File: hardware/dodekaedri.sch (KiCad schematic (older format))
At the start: 0 parts

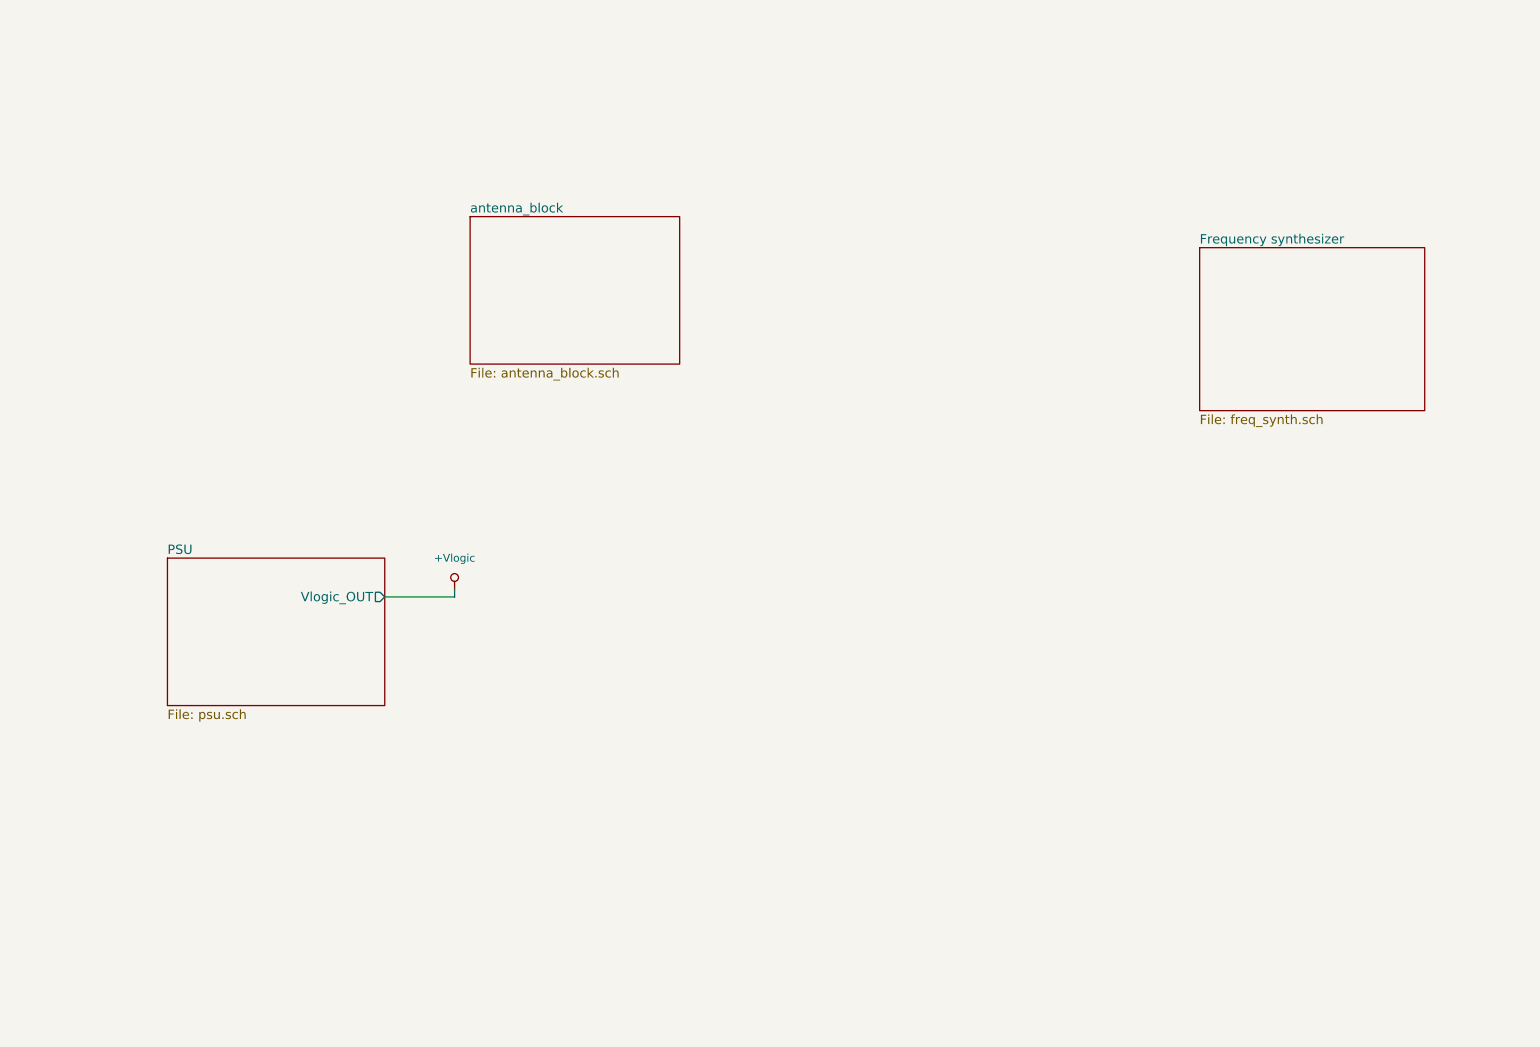
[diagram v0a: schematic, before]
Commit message: added rx/tx wm8731 (adc/dac)
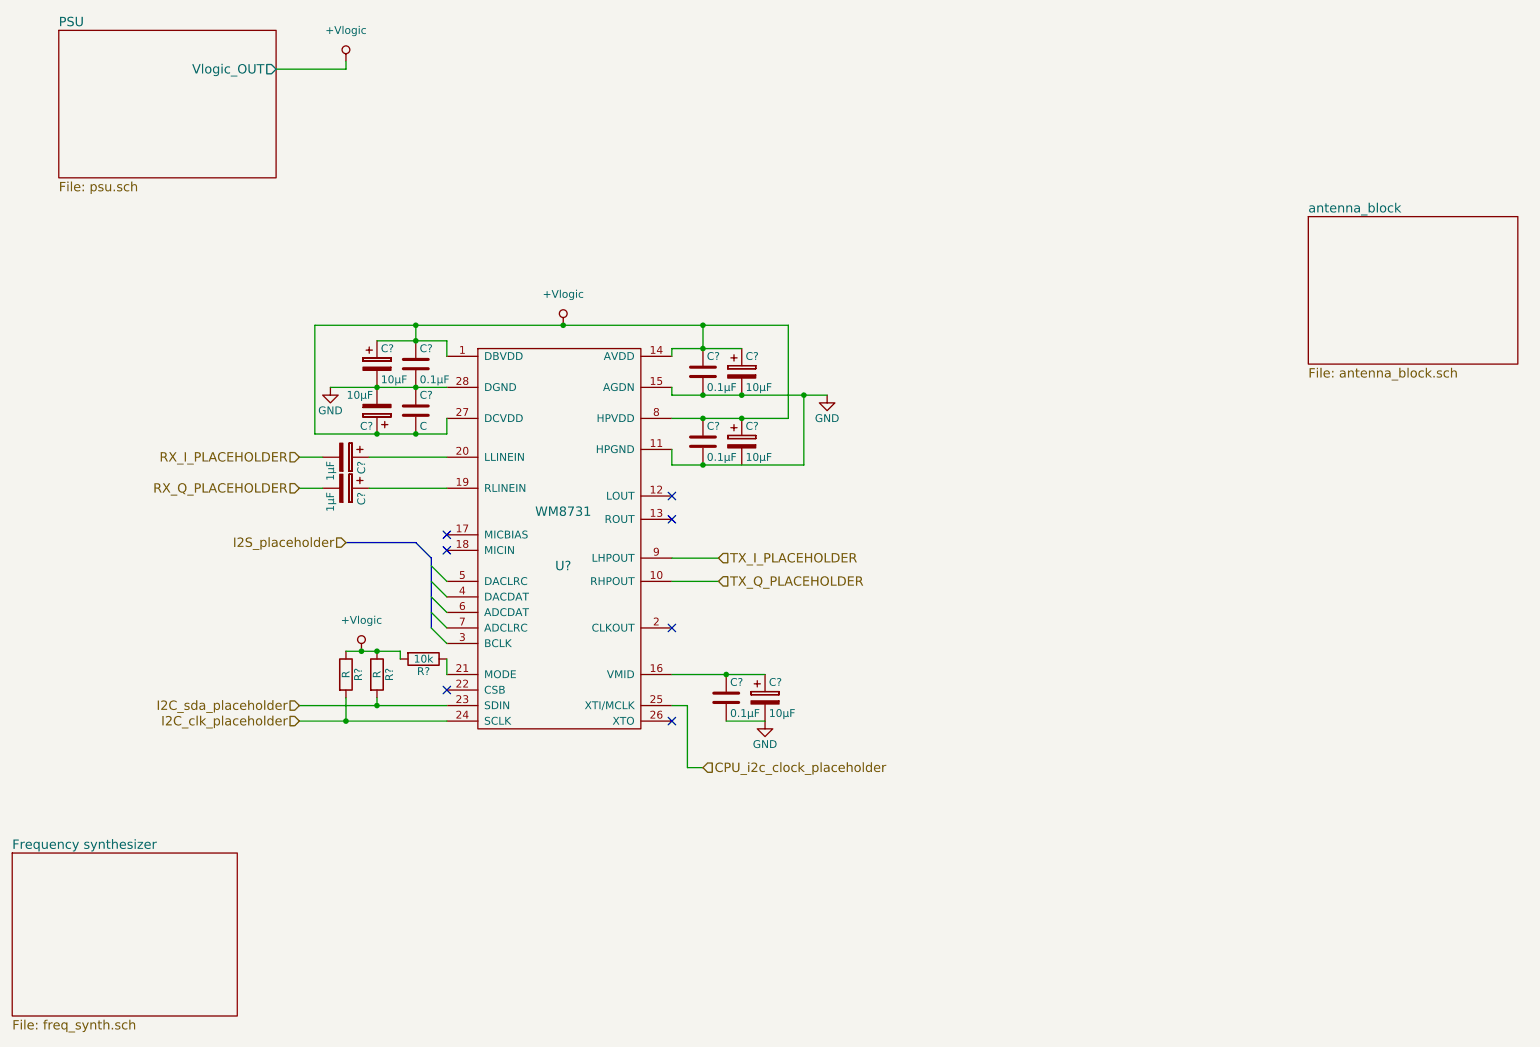
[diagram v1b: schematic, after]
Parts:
- added C? (x5): 10µF, symbol CP
- added C? (x2): 1µF, symbol CP
- added C? (x4): 0.1µF, symbol C
- added C?: C, symbol C
- added R? (x2): R, symbol R
- added R?: 10k, symbol R
- added U?: WM8731, symbol WM8731
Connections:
- net +Vlogic: now also C?.1, C?.1, C?.1, C?.1, C?.1, C?.1, C?.1, C?.2, R?.1, R?.1, R?.2, U?.1 (DBVDD), U?.14 (AVDD), U?.27 (DCVDD), U?.8 (HPVDD)
- new net: C?.1, C?.1, U?.16 (VMID)
- new net: C?.1, U?.19 (RLINEIN)
- new net: C?.1, U?.20 (LLINEIN)
- new net: R?.1, U?.21 (MODE)
- new net CPU_i2c_clock_placeholder: U?.25 (XTI/MCLK)
- new net GND: C?.1, C?.2, C?.2, C?.2, C?.2, C?.2, C?.2, C?.2, C?.2, U?.11 (HPGND), U?.15 (AGDN), U?.28 (DGND)
- new net I2C_clk_placeholder: R?.2, U?.24 (SCLK)
- new net I2C_sda_placeholder: R?.2, U?.23 (SDIN)
- new net RX_I_PLACEHOLDER: C?.2
- new net RX_Q_PLACEHOLDER: C?.2
- new net TX_I_PLACEHOLDER: U?.9 (LHPOUT)
- new net TX_Q_PLACEHOLDER: U?.10 (RHPOUT)
- no-connect marks 0 -> 7

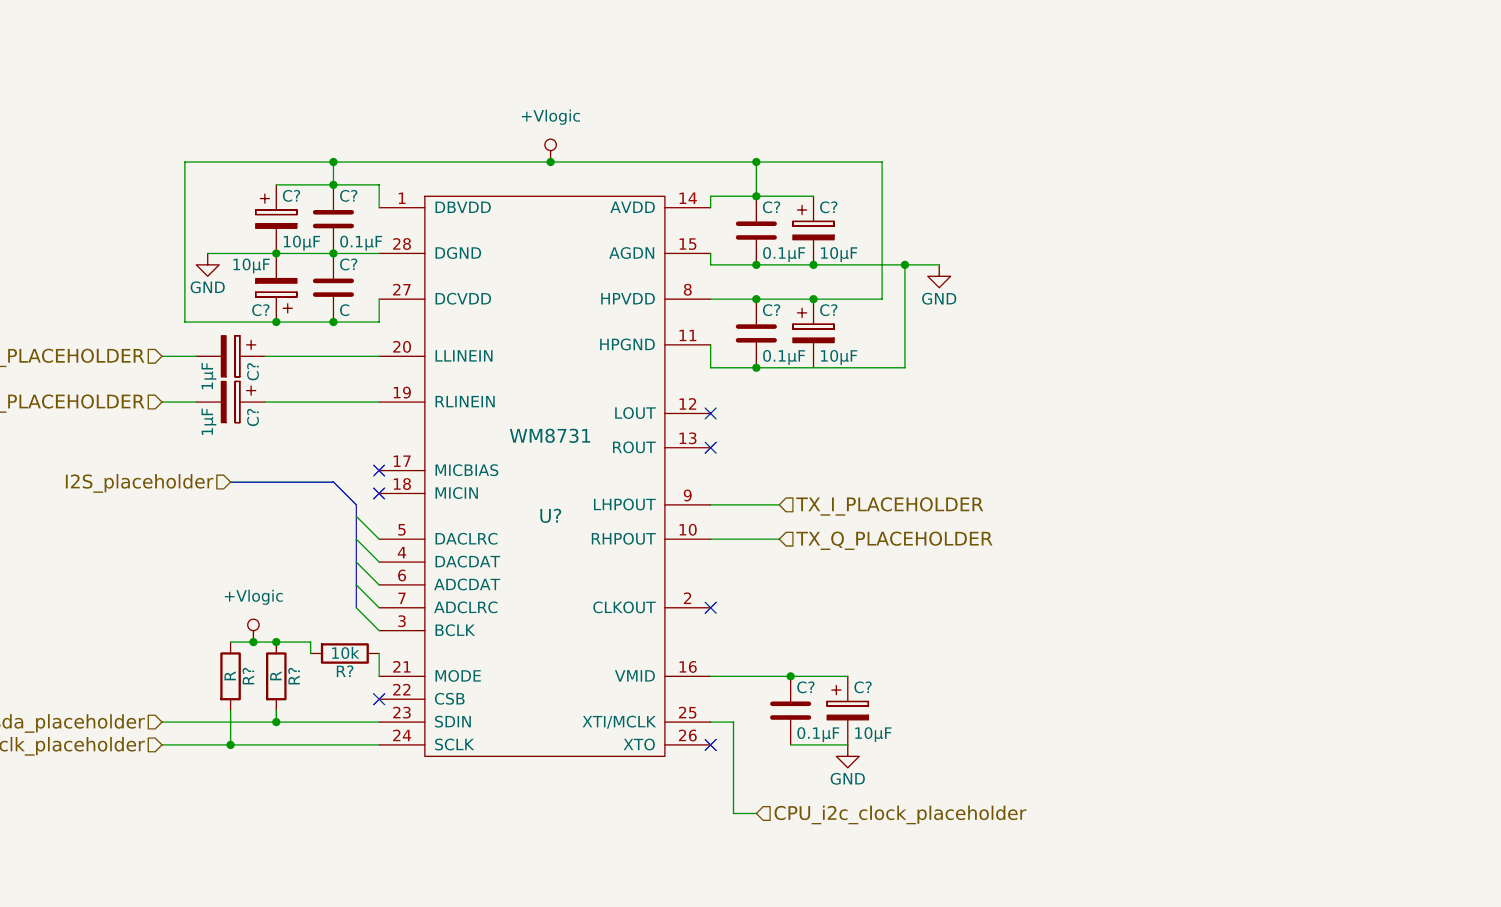
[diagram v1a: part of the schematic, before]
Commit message: Added TX chain schematic block and Vin netlist for input power_flag
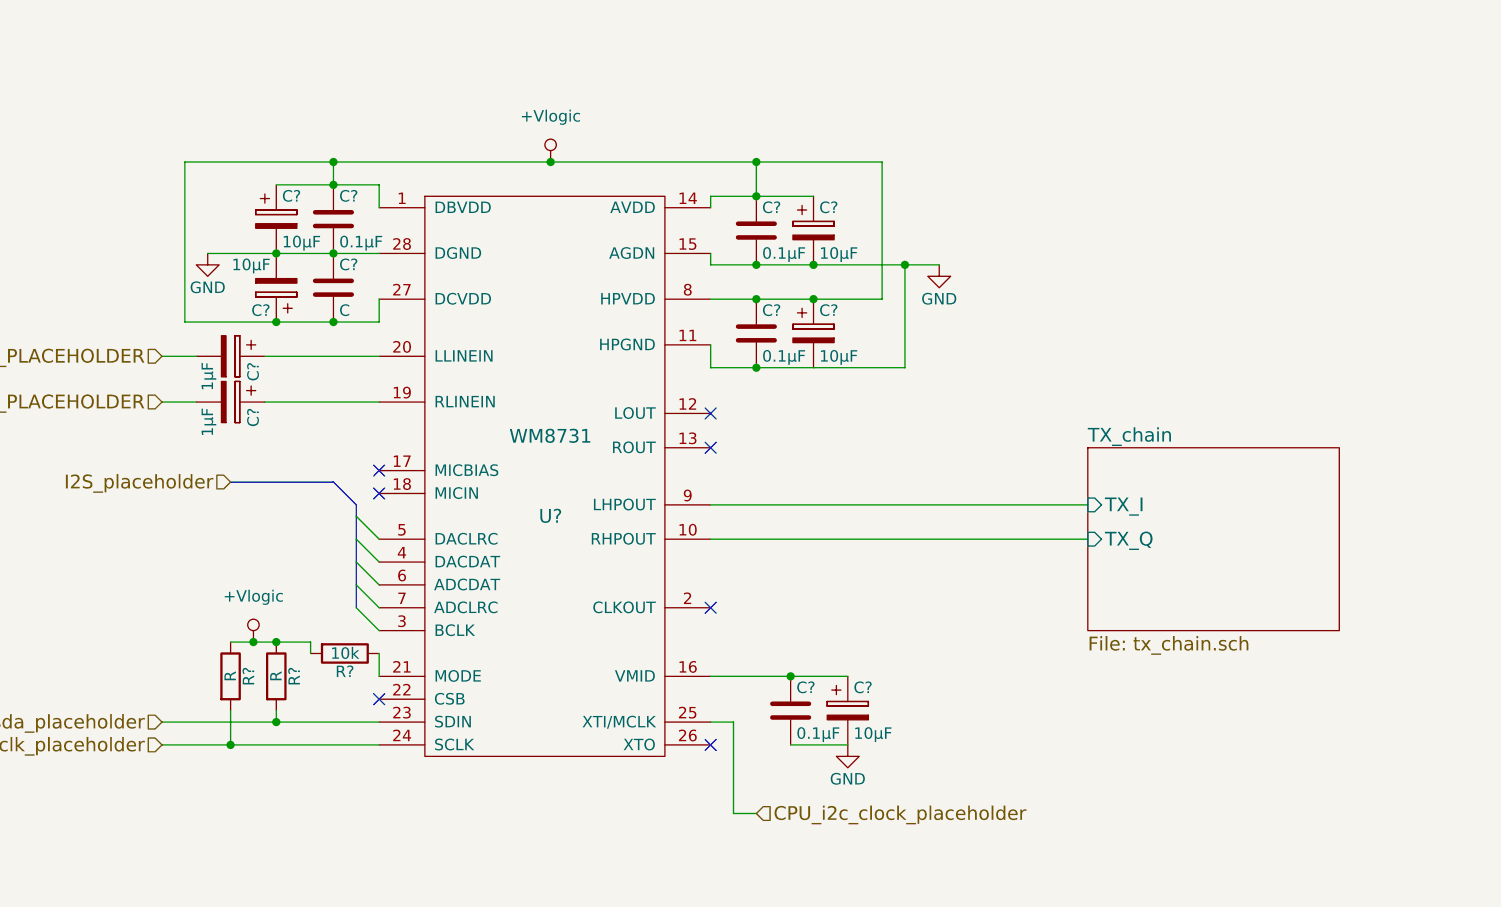
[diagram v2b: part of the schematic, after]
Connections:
- net TX_I_PLACEHOLDER renamed TX_chain/TX_I
- net TX_Q_PLACEHOLDER renamed TX_chain/TX_Q
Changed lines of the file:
@@
 $Descr A4 11693 8268
 encoding utf-8
-Sheet 1 4
+Sheet 1 5
 Title "Block layer"
 Date "2016-09-20"
@@
 	3000 1250 3000 1200
 Wire Wire Line
-	2900 3300 3650 3300
+	2900 3300 3200 3300
+Wire Wire Line
+	3200 3300 3450 3300
+Wire Wire Line
+	3450 3300 3650 3300
 Wire Wire Line
 	3650 3750 3150 3750
@@
 	3650 3000 3650 3100
 Wire Wire Line
-	3200 3000 3650 3000
+	3200 3000 3450 3000
+Wire Wire Line
+	3450 3000 3650 3000
 Connection ~ 3450 3000
 Wire Wire Line
 	3450 3000 3450 2900
 Wire Wire Line
-	2800 2900 5850 2900
+	2800 2900 3450 2900
+Wire Wire Line
+	3450 2900 4400 2900
+Wire Wire Line
+	4400 2900 5300 2900
+Wire Wire Line
+	5300 2900 5850 2900
 Connection ~ 3200 3300
 Connection ~ 3450 3300
@@
 Connection ~ 4400 2900
 Wire Wire Line
-	5100 3050 5550 3050
+	5100 3050 5300 3050
+Wire Wire Line
+	5300 3050 5550 3050
 Wire Wire Line
 	5100 3050 5100 3100
 Connection ~ 5300 3050
 Wire Wire Line
-	5100 3350 6100 3350
+	5100 3350 5300 3350
+Wire Wire Line
+	5300 3350 5550 3350
+Wire Wire Line
+	5550 3350 5950 3350
+Wire Wire Line
+	5950 3350 6100 3350
 Wire Wire Line
 	5100 3350 5100 3300
@@
 	5850 2900 5850 3500
 Wire Wire Line
-	5850 3500 5100 3500
+	5850 3500 5550 3500
+Wire Wire Line
+	5550 3500 5300 3500
+Wire Wire Line
+	5300 3500 5100 3500
 Connection ~ 5300 2900
 Connection ~ 5550 3500
@@
 	5100 3700 5100 3800
 Wire Wire Line
-	5100 3800 5950 3800
+	5100 3800 5300 3800
+Wire Wire Line
+	5300 3800 5950 3800
 Wire Wire Line
 	5950 3800 5950 3350
@@
 NoConn ~ 3650 4350
 Wire Wire Line
-	2800 3600 3650 3600
+	2800 3600 3200 3600
+Wire Wire Line
+	3200 3600 3450 3600
+Wire Wire Line
+	3450 3600 3650 3600
 Wire Wire Line
 	3650 3600 3650 3500
@@
 NoConn ~ 3650 5250
 Wire Wire Line
-	2700 5350 3650 5350
+	2700 5350 3200 5350
+Wire Wire Line
+	3200 5350 3650 5350
 Wire Wire Line
 	3200 5350 3200 5300
 Wire Wire Line
-	2700 5450 3650 5450
+	2700 5450 3000 5450
+Wire Wire Line
+	3000 5450 3650 5450
 Wire Wire Line
 	3000 5450 3000 5300
 Wire Wire Line
-	3000 5000 3350 5000
+	3000 5000 3100 5000
+Wire Wire Line
+	3100 5000 3200 5000
+Wire Wire Line
+	3200 5000 3350 5000
 Connection ~ 3100 5000
 $Comp
@@
 $EndComp
 Wire Wire Line
-	5100 5150 5700 5150
+	5100 5150 5450 5150
+Wire Wire Line
+	5450 5150 5700 5150
 Connection ~ 5450 5150
 Wire Wire Line
@@
 	3450 4300 3550 4400
 Wire Bus Line
-	3550 4400 3550 4850
+	3550 4400 3550 4450
+Wire Bus Line
+	3550 4450 3550 4550
+Wire Bus Line
+	3550 4550 3550 4650
+Wire Bus Line
+	3550 4650 3550 4750
+Wire Bus Line
+	3550 4750 3550 4850
 Wire Bus Line
 	3450 4300 3000 4300
@@
 Wire Wire Line
 	5200 5750 5300 5750
-Text HLabel 5400 4400 2    60   Input ~ 0
-TX_I_PLACEHOLDER
-Text HLabel 5400 4550 2    60   Input ~ 0
-TX_Q_PLACEHOLDER
-Wire Wire Line
-	5100 4400 5400 4400
-Wire Wire Line
-	5100 4550 5400 4550
 $Comp
 L R R?
@@
 Wire Wire Line
 	2700 3950 2850 3950
+$Sheet
+S 6750 4150 1100 800
+U 57E42B3F
+F0 "TX_chain" 60
+F1 "tx_chain.sch" 60
+F2 "TX_I" I L 6750 4400 60
+F3 "TX_Q" I L 6750 4550 60
+$EndSheet
+Wire Wire Line
+	5100 4400 6750 4400
+Wire Wire Line
+	5100 4550 6750 4550
 $EndSCHEMATC

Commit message: honed multiple schematics
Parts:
- removed C? (x2): 1µF, symbol CP
- removed R?: 10k, symbol R
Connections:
- net GND: now also U?.22 (CSB)
- net RX_I_PLACEHOLDER: now also U?.20 (LLINEIN)
- net RX_Q_PLACEHOLDER: now also U?.19 (RLINEIN)
- no-connect marks 7 -> 16
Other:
- note added: "i2c=0x1A"
- moved on the sheet: C?, R?, U?
